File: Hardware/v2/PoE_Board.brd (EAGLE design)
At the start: 84.6 x 72.1 mm, 93 parts, among them U1 EDISON_CONNECTOR_FULLMOUNTING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, U2 LAN9512-JZX, U3 MAX4995AAUT+, U4 EDISON_CONNECTOR_FULLHEADER

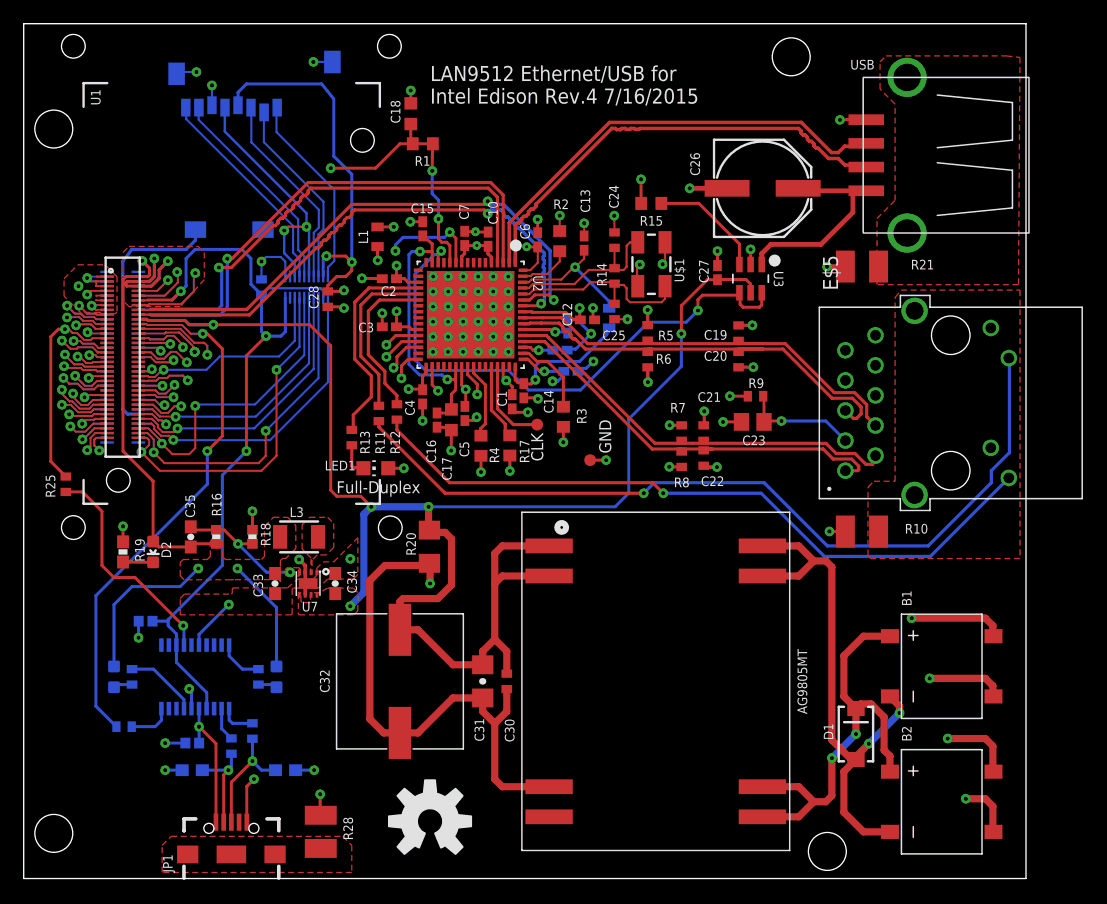
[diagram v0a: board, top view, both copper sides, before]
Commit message: Fixed some stuff from DRC
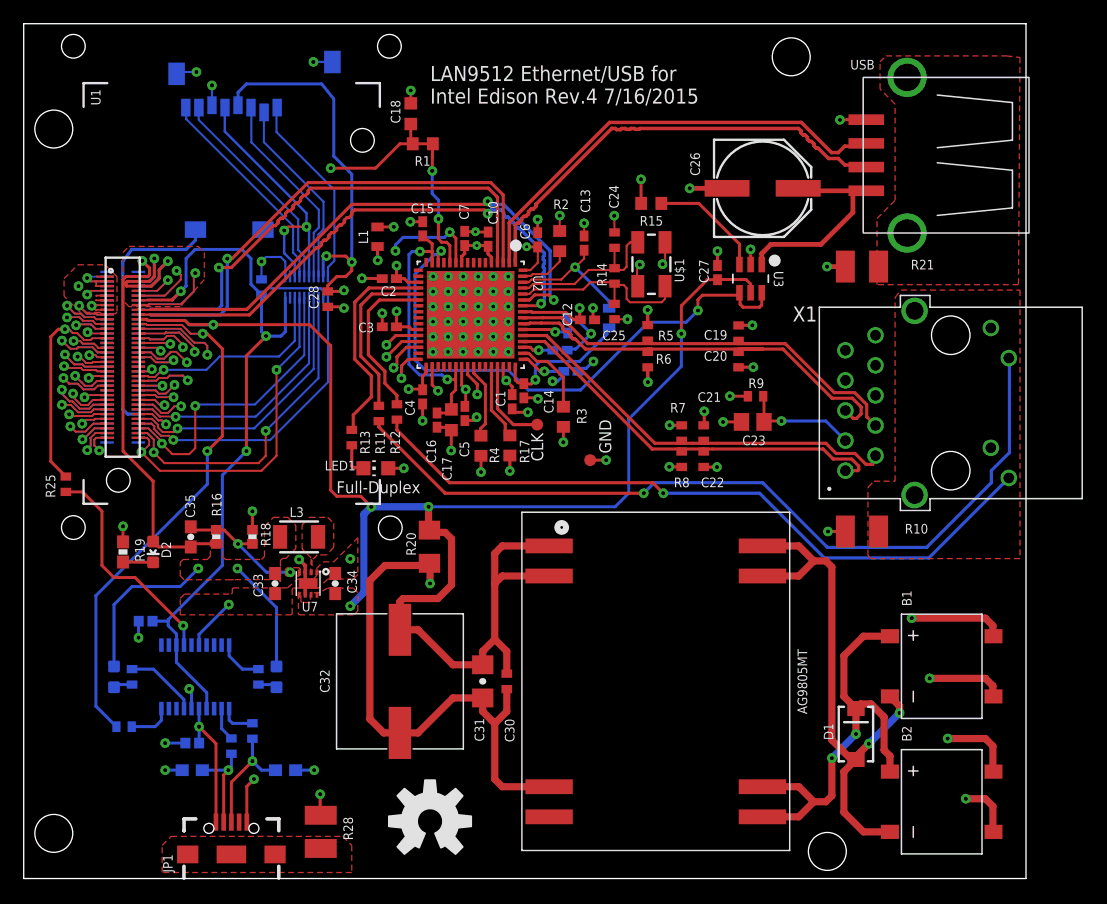
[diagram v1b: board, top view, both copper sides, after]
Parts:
- moved C22 0.10 mm to (56.1, 35.4)
- renumbered E$5 to X1
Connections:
- net S$8 renamed VBUS1
- removed net S$10: U4.61
- removed net S$5: U4.70
- removed net S$6: U4.20
- removed net S$7: U4.68
- removed net S$9: U1.53
- net 3_A2_SDDAT3: now also U4.68
- net 7_A6_SDDAT1: now also U4.70
- net P37: now also U1.37
- net P41: now also U1.41
- net P43: now also U1.43
- net P47: now also U4.47
- net P53: now also U1.53
- net P61: now also U4.61
- net USB_VBUS: now also U4.20
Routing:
- net GP28_I2C_6_SDA: track 7.63 -> 0.00 mm, vias 1 -> 0
- net P47: track 0.83 -> 8.43 mm, vias 0 -> 1
- net S$9: track 7.10 -> 0.00 mm, vias 1 -> 0
- net P53: track 0.51 -> 7.23 mm, vias 0 -> 1
- net P61\: track 4.30 -> 0.00 mm, vias 1 -> 0
- net P61: track 0.66 -> 4.56 mm, vias 0 -> 1
- net VDD3IO: track 147.0 -> 147.6 mm
- net RX_N: track 35.3 -> 34.7 mm
- net P26: vias 2 -> 1

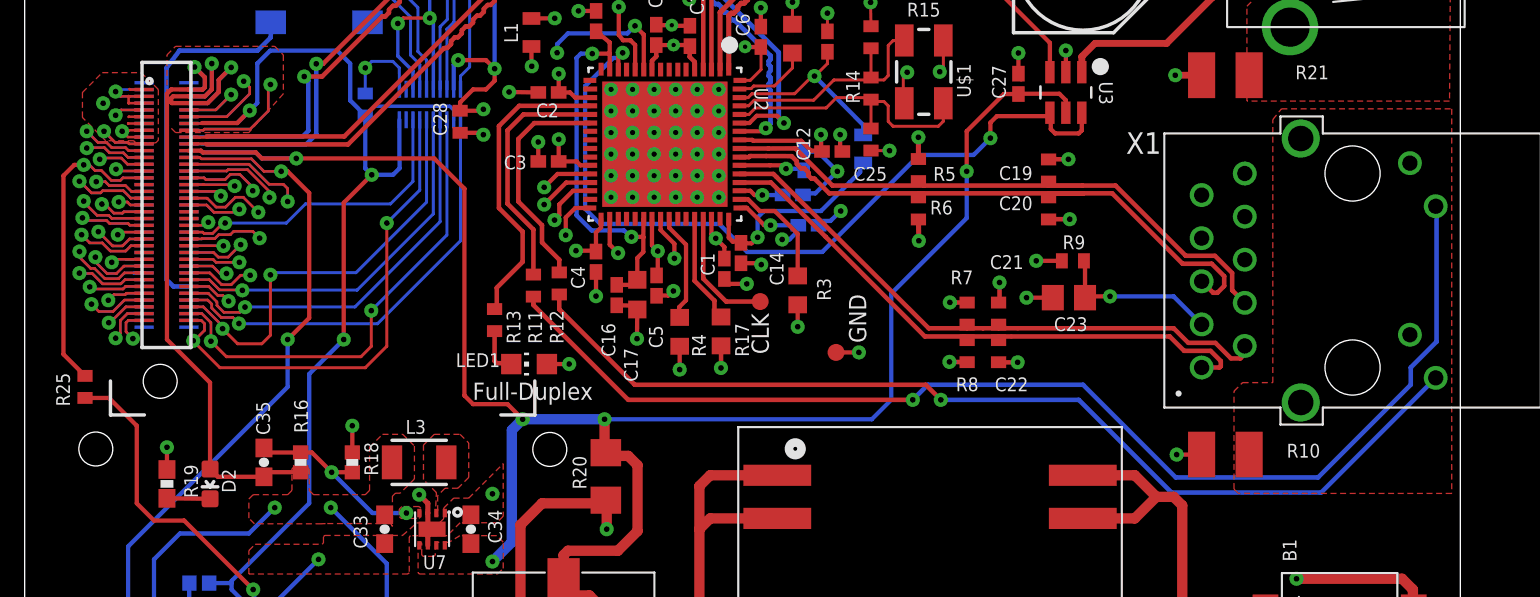
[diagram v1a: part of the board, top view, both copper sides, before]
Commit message: Got rid of unrouted airwires
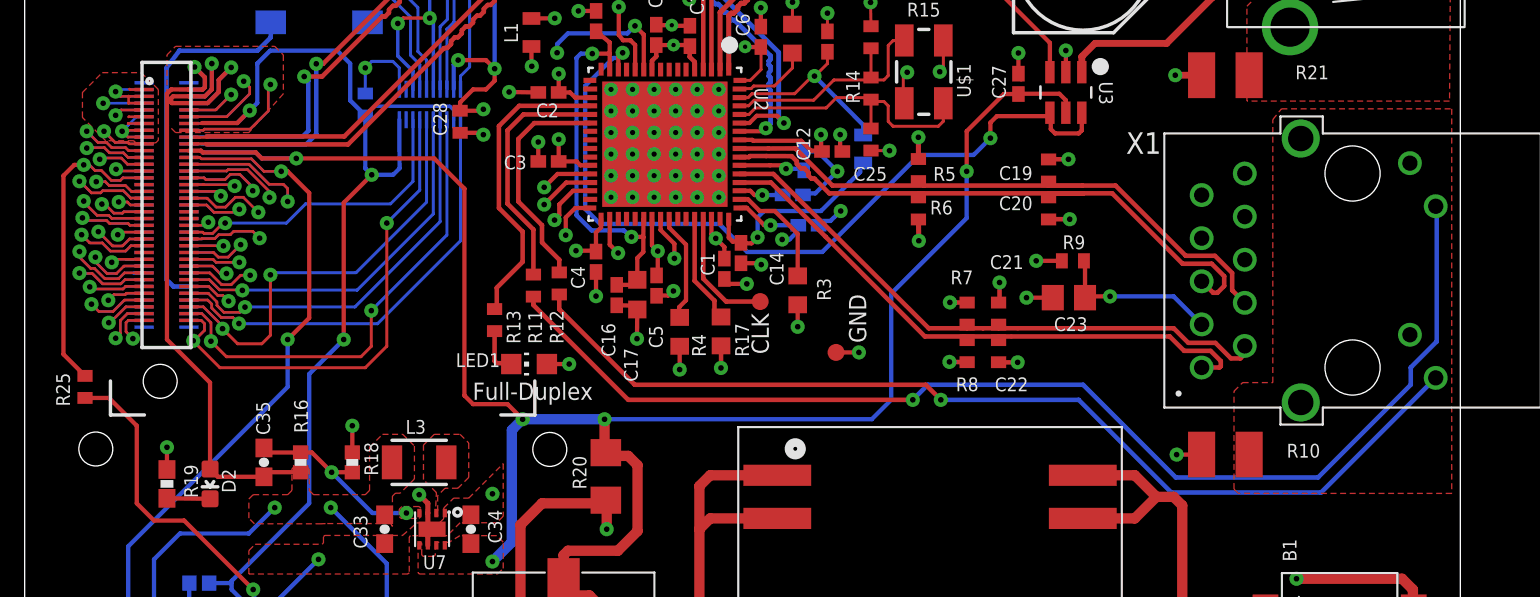
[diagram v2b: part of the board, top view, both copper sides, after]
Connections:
- new net S$5: AG9805MT.P$3, C30.1, C31.1, C32.1, R20.1
- net GND: no longer AG9805MT.P$3, C30.1, C31.1, C32.1, R20.1
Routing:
- net S$5: track 0.00 -> 44.2 mm
- net GND: track 183.6 -> 147.3 mm
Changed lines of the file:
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@@
 <grid distance="5" unitdist="mil" unit="mil" style="lines" multiple="1" display="yes" altdistance="0.25" altunitdist="mil" altunit="mil"/>
 <layers>
-<layer number="1" name="Top" color="4" fill="1" visible="yes" active="yes"/>
+<layer number="1" name="Top" color="4" fill="1" visible="no" active="yes"/>
 <layer number="2" name="gnd" color="11" fill="3" visible="yes" active="yes"/>
 <layer number="3" name="pwr" color="13" fill="3" visible="yes" active="yes"/>
@@
 <wire x1="23.4442" y1="53.2384" x2="17.78" y2="47.56" width="0.27" layer="1"/>
 </signal>
+<signal name="S$5">
+<contactref element="AG9805MT" pad="P$3"/>
+<wire x1="43.07" y1="7.747" x2="39.116" y2="7.747" width="0.6096" layer="1"/>
+<contactref element="C30" pad="1"/>
+<wire x1="39.37" y1="15.86" x2="39.497" y2="15.987" width="0.27" layer="1"/>
+<wire x1="39.497" y1="14.097" x2="39.497" y2="15.987" width="0.6096" layer="1"/>
+<wire x1="39.116" y1="7.747" x2="38.481" y2="8.382" width="0.6096" layer="1"/>
+<wire x1="38.481" y1="8.382" x2="38.481" y2="13.081" width="0.6096" layer="1"/>
+<wire x1="38.481" y1="13.081" x2="39.497" y2="14.097" width="0.6096" layer="1"/>
+<contactref element="R20" pad="1"/>
+<wire x1="37.465" y1="14.097" x2="38.481" y2="13.081" width="0.6096" layer="1"/>
+<contactref element="C31" pad="1"/>
+<wire x1="37.465" y1="15.237" x2="37.465" y2="14.097" width="0.6096" layer="1"/>
+<wire x1="32.786" y1="26.416" x2="32.97" y2="26.6" width="0.6096" layer="1"/>
+<wire x1="29.21" y1="26.416" x2="32.786" y2="26.416" width="0.6096" layer="1"/>
+<wire x1="34.954" y1="15.237" x2="37.465" y2="15.237" width="0.6096" layer="1"/>
+<wire x1="34.954" y1="15.237" x2="32.004" y2="12.287" width="0.6096" layer="1"/>
+<wire x1="27.94" y1="25.146" x2="29.21" y2="26.416" width="0.6096" layer="1"/>
+<wire x1="27.94" y1="13.462" x2="27.94" y2="25.146" width="0.6096" layer="1"/>
+<contactref element="C32" pad="1"/>
+<wire x1="32.004" y1="12.287" x2="30.48" y2="12.287" width="0.6096" layer="1"/>
+<wire x1="30.48" y1="12.287" x2="29.115" y2="12.287" width="0.6096" layer="1"/>
+<wire x1="29.115" y1="12.287" x2="27.94" y2="13.462" width="0.6096" layer="1"/>
+</signal>
 <signal name="GND">
 <contactref element="U1" pad="1"/>
@@
 <contactref element="U$1" pad="2"/>
 <contactref element="U$1" pad="4"/>
-<contactref element="U4" pad="13"/>
-<contactref element="U4" pad="15"/>
 <contactref element="U4" pad="1"/>
-<contactref element="U4" pad="5"/>
-<contactref element="U4" pad="9"/>
-<contactref element="U4" pad="11"/>
 <contactref element="U3" pad="2"/>
 <contactref element="C26" pad="-"/>
@@
 <wire x1="4.2084" y1="50.7928" x2="4.0886" y2="50.673" width="0.1524" layer="16"/>
 <wire x1="5.7666" y1="50.3928" x2="4.3688" y2="50.3928" width="0.1524" layer="16"/>
-<wire x1="5.7666" y1="49.1928" x2="5.327" y2="49.1928" width="0.1524" layer="16"/>
 <wire x1="37.9222" y1="54.5496" x2="36.8904" y2="54.5496" width="0.254" layer="1"/>
 <wire x1="36.8904" y1="54.5496" x2="36.8554" y2="54.5846" width="0.254" layer="1"/>
@@
 <wire x1="50.8254" y1="59.0042" x2="50.8254" y2="56.9858" width="0.254" layer="1"/>
 <wire x1="50.8254" y1="56.9858" x2="50.839" y2="56.9722" width="0.254" layer="1"/>
-<contactref element="AG9805MT" pad="P$3"/>
-<wire x1="43.07" y1="7.747" x2="39.116" y2="7.747" width="0.6096" layer="1"/>
-<contactref element="C30" pad="1"/>
-<wire x1="39.37" y1="15.86" x2="39.497" y2="15.987" width="0.27" layer="1"/>
-<wire x1="39.497" y1="14.097" x2="39.497" y2="15.987" width="0.6096" layer="1"/>
-<wire x1="39.116" y1="7.747" x2="38.481" y2="8.382" width="0.6096" layer="1"/>
 <via x="33.02" y="24.892" extent="1-16" drill="0.3302"/>
-<wire x1="38.481" y1="8.382" x2="38.481" y2="13.081" width="0.6096" layer="1"/>
-<wire x1="38.481" y1="13.081" x2="39.497" y2="14.097" width="0.6096" layer="1"/>
-<wire x1="37.465" y1="14.097" x2="38.481" y2="13.081" width="0.6096" layer="1"/>
 <via x="26.289" y="26.9748" extent="1-16" drill="0.3302"/>
-<contactref element="C31" pad="1"/>
-<wire x1="37.465" y1="15.237" x2="37.465" y2="14.097" width="0.6096" layer="1"/>
-<wire x1="34.954" y1="15.237" x2="37.465" y2="15.237" width="0.6096" layer="1"/>
-<wire x1="27.94" y1="25.146" x2="29.21" y2="26.416" width="0.6096" layer="1"/>
-<wire x1="27.94" y1="13.462" x2="27.94" y2="25.146" width="0.6096" layer="1"/>
-<contactref element="C32" pad="1"/>
-<wire x1="30.48" y1="12.287" x2="29.115" y2="12.287" width="0.6096" layer="1"/>
-<wire x1="29.115" y1="12.287" x2="27.94" y2="13.462" width="0.6096" layer="1"/>
 <via x="7.112" y="29.718" extent="1-16" drill="0.3302"/>
 <contactref element="R19" pad="1"/>
@@
 <contactref element="U7" pad="1"/>
 <contactref element="C34" pad="1"/>
-<contactref element="R20" pad="1"/>
 <wire x1="32.9565" y1="26.416" x2="33.02" y2="26.3525" width="0.6096" layer="1"/>
 <wire x1="33.02" y1="26.3525" x2="33.02" y2="24.892" width="0.6096" layer="1"/>
-<wire x1="29.21" y1="26.416" x2="32.786" y2="26.416" width="0.6096" layer="1"/>
-<wire x1="32.786" y1="26.416" x2="32.97" y2="26.6" width="0.6096" layer="1"/>
-<wire x1="34.954" y1="15.237" x2="32.004" y2="12.287" width="0.6096" layer="1"/>
-<wire x1="32.004" y1="12.287" x2="30.48" y2="12.287" width="0.6096" layer="1"/>
-<wire x1="5.7646" y1="48.393" x2="5.7666" y2="48.3928" width="0" layer="19" extent="1-16"/>
-<wire x1="5.7666" y1="49.9928" x2="5.7646" y2="49.993" width="0" layer="19" extent="1-16"/>
-<wire x1="5.7666" y1="48.7928" x2="5.7646" y2="48.793" width="0" layer="19" extent="1-16"/>
-<wire x1="5.7666" y1="49.1928" x2="5.7646" y2="49.193" width="0" layer="19" extent="1-16"/>
-<wire x1="5.7666" y1="47.9928" x2="5.7646" y2="47.993" width="0" layer="19" extent="1-16"/>
-<wire x1="32.786" y1="26.416" x2="32.9565" y2="26.416" width="0" layer="19" extent="1-1"/>
+<contactref element="U4" pad="9"/>
+<contactref element="U4" pad="11"/>
+<contactref element="U4" pad="13"/>
+<contactref element="U4" pad="15"/>
+<wire x1="5.7666" y1="49.1928" x2="5.327" y2="49.1928" width="0.1524" layer="16"/>
+<wire x1="5.327" y1="49.1928" x2="4.4704" y2="48.3362" width="0.1524" layer="16"/>
+<wire x1="5.7666" y1="48.7928" x2="4.927" y2="48.7928" width="0.1524" layer="16"/>
+<wire x1="4.927" y1="48.7928" x2="4.4704" y2="48.3362" width="0.1524" layer="16"/>
+<wire x1="5.7666" y1="48.3928" x2="4.527" y2="48.3928" width="0.1524" layer="16"/>
+<wire x1="4.527" y1="48.3928" x2="4.4704" y2="48.3362" width="0.1524" layer="16"/>
+<wire x1="5.7666" y1="47.9928" x2="4.8138" y2="47.9928" width="0.1524" layer="16"/>
+<wire x1="4.8138" y1="47.9928" x2="4.4704" y2="48.3362" width="0.1524" layer="16"/>
+<contactref element="U4" pad="5"/>
+<wire x1="5.7666" y1="49.9928" x2="3.3528" y2="49.9872" width="0.1524" layer="16"/>
 </signal>
 <signal name="N$1">
@@
 <wire x1="52.705" y1="32.512" x2="60.833" y2="32.512" width="0.27" layer="16"/>
 <wire x1="60.833" y1="32.512" x2="66.294" y2="27.051" width="0.27" layer="16"/>
-<wire x1="66.294" y1="27.051" x2="75.11415" y2="27.051" width="0.27" layer="16"/>
-<wire x1="75.11415" y1="27.051" x2="81.87055" y2="33.8074" width="0.27" layer="16"/>
 <contactref element="X1" pad="L4"/>
 <wire x1="30.226" y1="37.846" x2="34.671" y2="33.401" width="0.27" layer="1"/>
 <wire x1="34.671" y1="33.401" x2="51.816" y2="33.401" width="0.27" layer="1"/>
 <wire x1="51.816" y1="33.401" x2="52.705" y2="32.512" width="0.27" layer="1"/>
-<wire x1="81.87055" y1="33.8074" x2="81.862" y2="33.807" width="0" layer="19" extent="16-16"/>
+<wire x1="66.294" y1="27.051" x2="75.106" y2="27.051" width="0.27" layer="16"/>
+<wire x1="75.106" y1="27.051" x2="81.862" y2="33.807" width="0.27" layer="16"/>
 </signal>
 <signal name="N$18">
@@
 <wire x1="3.556" y1="43.0784" x2="3.7338" y2="42.9006" width="0.1524" layer="1"/>
 <wire x1="3.7338" y1="42.9006" x2="4.826" y2="42.9006" width="0.1524" layer="1"/>
-<wire x1="4.826" y1="42.9006" x2="4.9276" y2="42.799" width="0.1524" layer="1"/>
-<wire x1="4.9276" y1="42.799" x2="5.715" y2="42.799" width="0.1524" layer="1"/>
 <wire x1="4.9276" y1="42.799" x2="5.7666" y2="42.7928" width="0.1524" layer="16"/>
 <contactref element="U1" pad="41"/>
-<wire x1="5.7666" y1="42.7928" x2="5.7646" y2="42.793" width="0" layer="19" extent="1-16"/>
+<wire x1="4.826" y1="42.9006" x2="4.9336" y2="42.793" width="0.1524" layer="1"/>
+<wire x1="4.9336" y1="42.793" x2="5.7646" y2="42.793" width="0.1524" layer="1"/>
 </signal>
 <signal name="P43">
